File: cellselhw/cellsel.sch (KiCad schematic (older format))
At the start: 51 parts

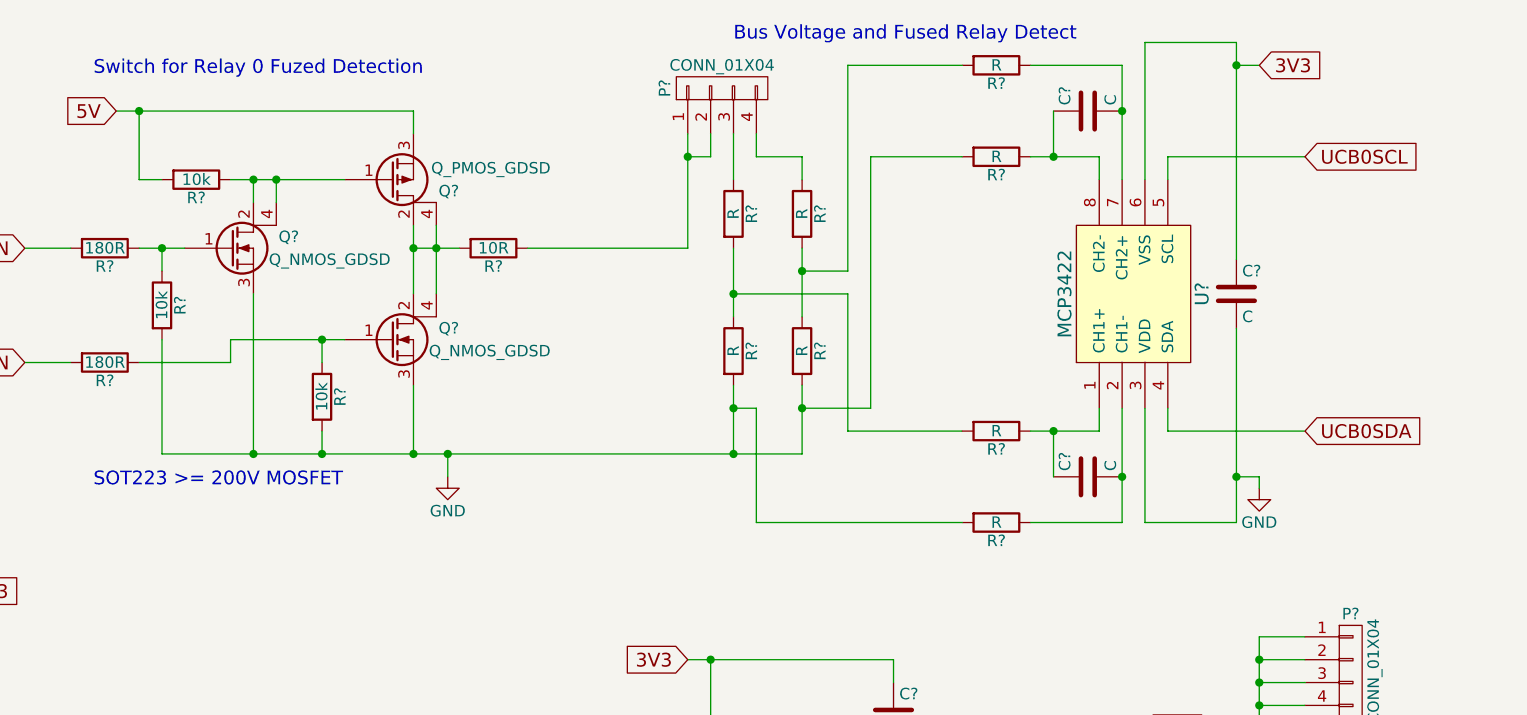
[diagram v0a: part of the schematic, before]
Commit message: Added bus discharge transistors
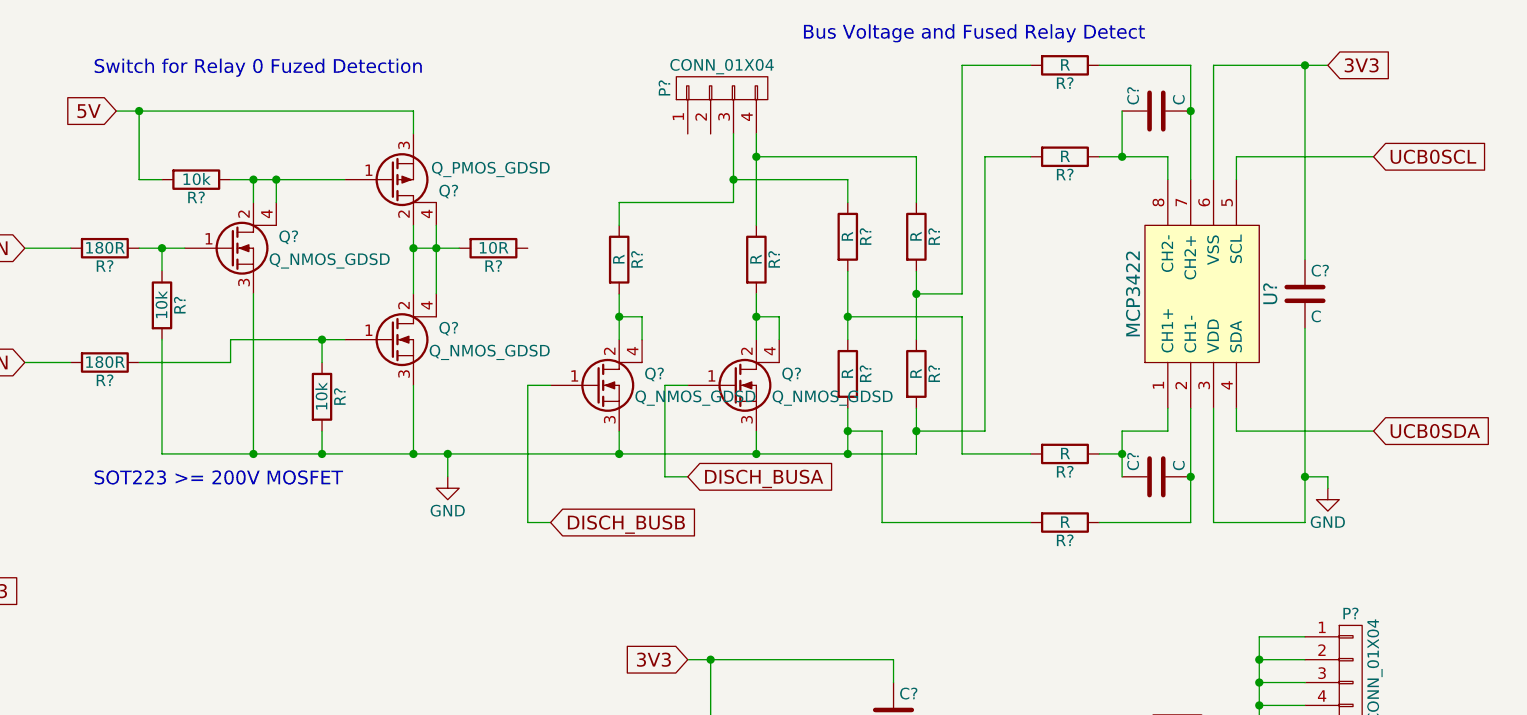
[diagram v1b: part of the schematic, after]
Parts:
- added Q? (x2): Q_NMOS_GDSD, symbol Q_NMOS_GDSD
- added R? (x2): R, symbol R
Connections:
- net GND: now also Q?.3 (S), Q?.3 (S)
- net at P?.3 (P3), R?.1: now also R?.1
- net at P?.4 (P4), R?.1: now also R?.1
- new net: Q?.2 (D), Q?.4 (D), R?.2 (x2)
- new net DISCH_BUSA: Q?.1 (G)
- new net DISCH_BUSB: Q?.1 (G)
- now unconnected: P?.1 (P1), P?.2 (P2), R?.1
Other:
- moved on the sheet: C?, R?, U?

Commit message: Schematic Complete
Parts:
- added P?: CONN_01X03, symbol CONN_01X03
- added P?: CONN_01X04, symbol CONN_01X04
- added R?: 4k7, symbol R
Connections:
- net 12V: now also P?.1 (P1), P?.2 (P2)
- net 3V3: now also P?.1 (P1), R?.1
- net DISCH_BUSA: now also U?.18 (P2.5)
- net DISCH_BUSB: now also U?.17 (P2.4)
- net GND: now also P?.3 (P3), P?.3 (P3), P?.4 (P4)
- net at U?.16 (P2.3): now also P?.2 (P2), R?.2
- net at R?.1: now also P?.1 (P1), P?.2 (P2)
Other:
- note added: "DS18B20"
- note added: "NCH SOT223 FET: IRLL110BPF (100V) / STN4NF20L (200V)\nPCH SOT223 FET: BSP220,115 (-220V)"
- moved on the sheet: C?, U?

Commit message: PCB Layout Stage 1
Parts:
- added C13: 100uF, Capacitors_SMD:C_1206, symbol CP1
- C1, C8: renamed from C?; value C -> 100nF; footprint (none) -> Capacitors_SMD:C_0603
- C10, C11: renamed from C?; footprint (none) -> Capacitors_SMD:C_0603
- C12, C14, C15, C5: renamed from C?; value C -> 1uF; footprint (none) -> Capacitors_SMD:C_0805
- C2: renamed from C?; footprint (none) -> Capacitors_SMD:C_1210
- C3, C4, C6, C7: renamed from C?; footprint (none) -> Capacitors_SMD:C_1206
- C9: renamed from C?; footprint (none) -> Capacitors_SMD:C_0805
- D1: renamed from D?; footprint (none) -> TO_SOT_Packages_SMD:SOT-23
- P1, P2, P3, P4, P8: renamed from P?; footprint (none) -> Connectors_Molex:Molex_KK-6410-04_04x2.54mm_Straight
- P5, P6: renamed from P?; footprint (none) -> Connectors_Molex:Molex_KK-6410-08_08x2.54mm_Straight
- P7: renamed from P?; footprint (none) -> Connectors_Molex:Molex_KK-6410-03_03x2.54mm_Straight
- Q1, Q2, Q3, Q4, Q5: renamed from Q?; footprint (none) -> TO_SOT_Packages_SMD:SOT-223
- R1, R15, R16, R2: renamed from R?; value R -> 10k; footprint (none) -> Resistors_SMD:R_0603
- R10, R11, R14, R17, R18, R19, R20, R21, R22, R3, R6: renamed from R?; footprint (none) -> Resistors_SMD:R_0603
- R12, R13: renamed from R?; value R -> 10k; footprint (none) -> RES_TH:PRECISION_RESISTOR_5MM
- R4, R5: renamed from R?; value R -> 500k; footprint (none) -> RES_TH:PRECISION_RESISTOR_5MM
- R7: renamed from R?; footprint (none) -> Resistors_SMD:R_0805
- R8, R9: renamed from R?; value R -> 1k; footprint (none) -> Resistors_SMD:R_0805
- U1, U3: renamed from U?; footprint (none) -> TO_SOT_Packages_SMD:SOT-223
- U2: renamed from U?; footprint (none) -> Housings_SOIC:SOIC-8_3.9x4.9mm_Pitch1.27mm
- U4: renamed from U?; footprint (none) -> Housings_SSOP:TSSOP-28_4.4x9.7mm_Pitch0.65mm
- U5, U7: renamed from U?; footprint (none) -> Housings_DIP:DIP-18_W7.62mm
- U6: renamed from U?; footprint (none) -> Housings_SOIC:SOIC-28W_7.5x17.9mm_Pitch1.27mm
- U8: renamed from U?; footprint (none) -> Housings_SOIC:SOIC-16W_7.5x10.3mm_Pitch1.27mm
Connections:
- net 12V: now also C13.1
- net GND: now also C13.2

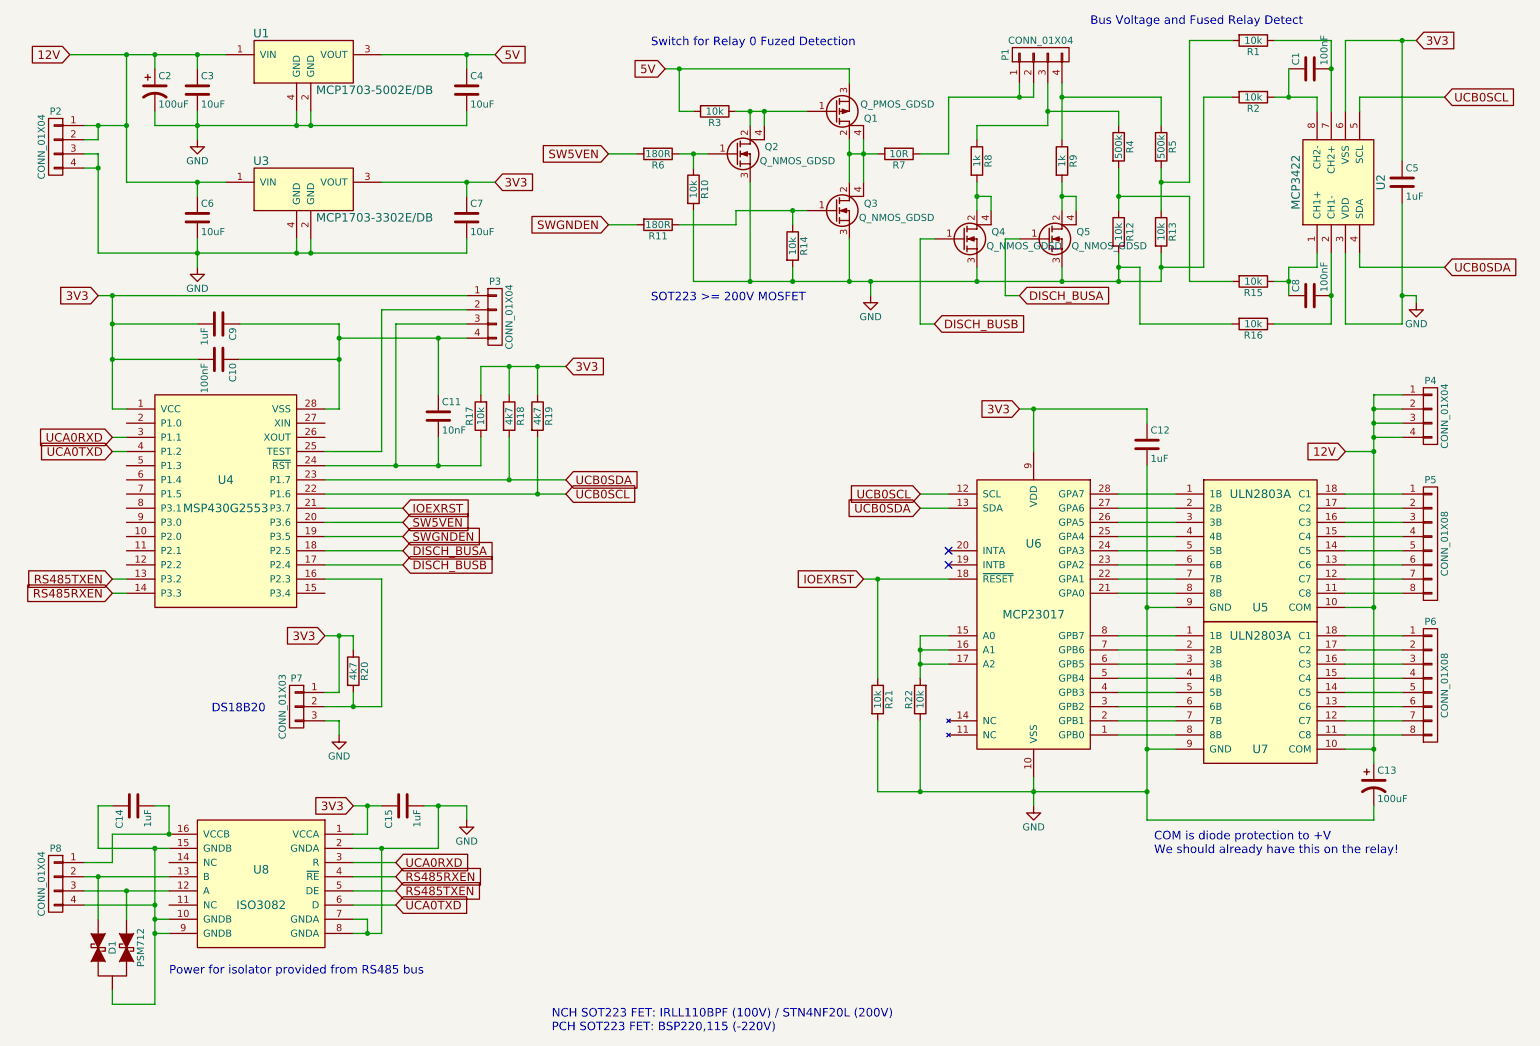
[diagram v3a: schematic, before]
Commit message: Finalused Transistor Selection
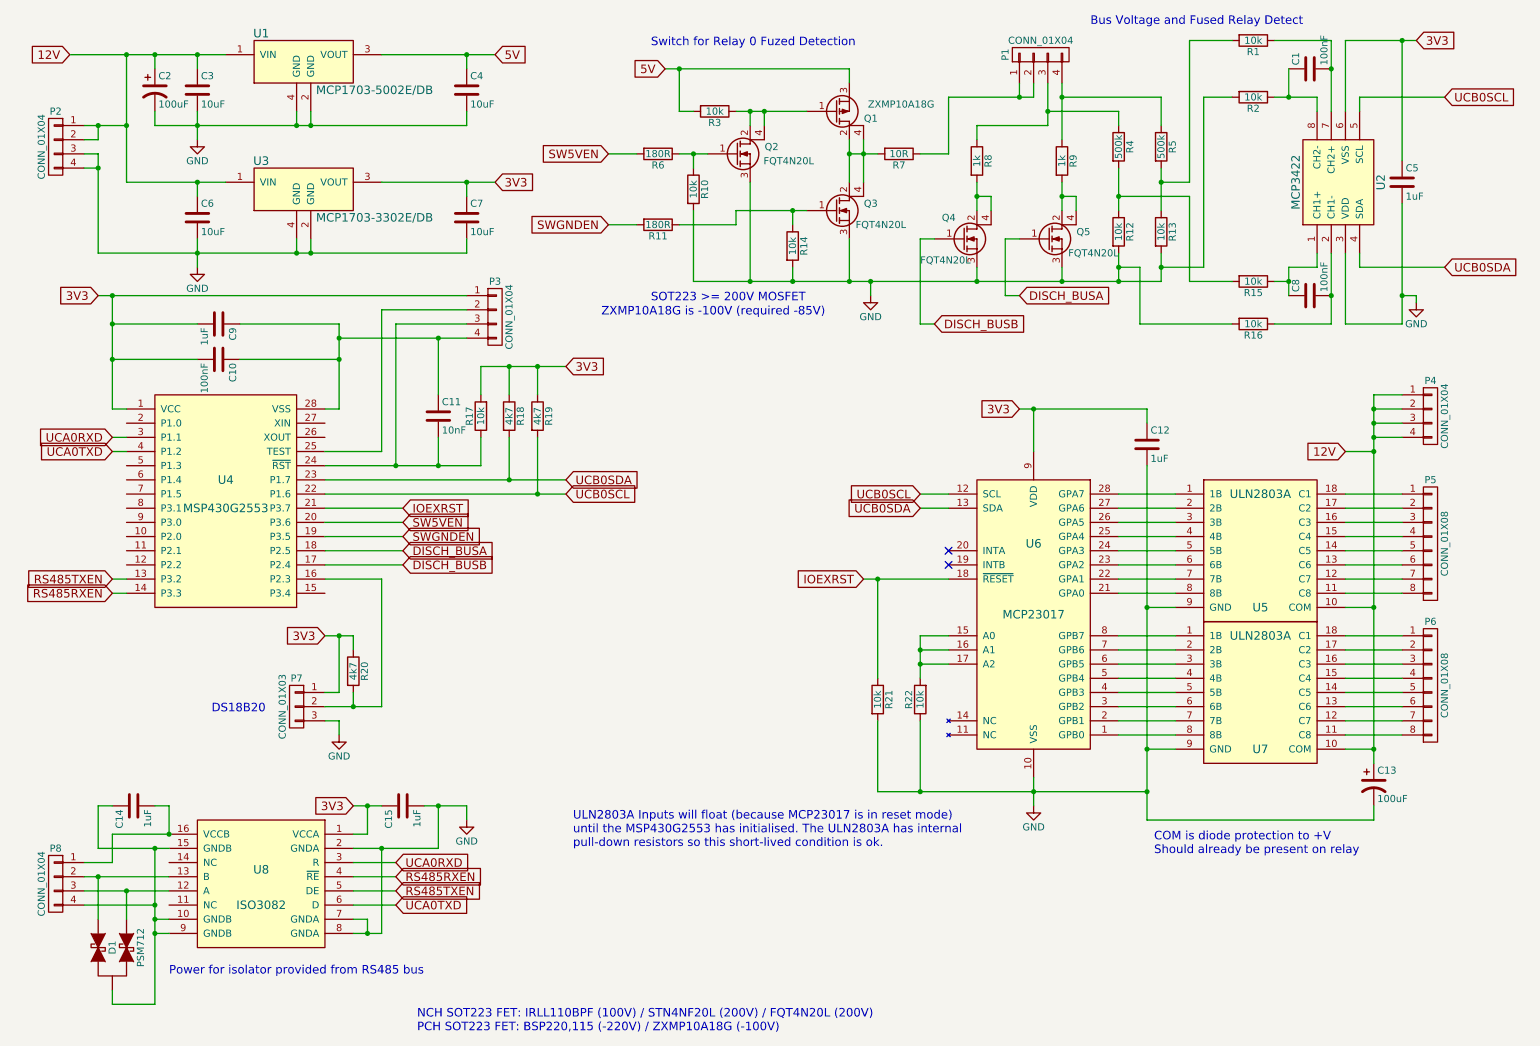
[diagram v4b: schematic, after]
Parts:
- Q1: value Q_PMOS_GDSD -> ZXMP10A18G
- Q2, Q3, Q4, Q5: value Q_NMOS_GDSD -> FQT4N20L
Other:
- note added: "COM is diode protection to +V\nShould already be present on relay"
- note added: "NCH SOT223 FET: IRLL110BPF (100V) / STN4NF20L (200V) / FQT4N20L (200V)\nPCH SOT223 FET: BSP220,115 (-220V) / ZXMP10A18G (-100V)"
- note added: "ULN2803A Inputs will float (because MCP23017 is in reset mode)\nuntil the MSP430G2553 has initialised. The ULN2803A has internal\npull-down resistors so this short-lived condition is ok."
- note added: "ZXMP10A18G is -100V (required -85V)"
- note removed: "COM is diode protection to +V\nWe should already have this on the relay!"
- note removed: "NCH SOT223 FET: IRLL110BPF (100V) / STN4NF20L (200V)\nPCH SOT223 FET: BSP220,115 (-220V)"
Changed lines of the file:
@@
 LIBS:contrib
 LIBS:valves
+LIBS:vreg
 LIBS:msp430
+LIBS:powerswitchics
+LIBS:ioexpanders
+LIBS:adcanddac
+LIBS:ti
+LIBS:transientsuppressor
 LIBS:cellsel-cache
 EELAYER 25 0
@@
 P 5500 1500
 F 0 "Q2" H 5800 1550 50  0000 R CNN
-F 1 "Q_NMOS_GDSD" H 6200 1450 50  0000 R CNN
+F 1 "FQT4N20L" H 6050 1450 50  0000 R CNN
 F 2 "TO_SOT_Packages_SMD:SOT-223" H 5700 1600 50  0001 C CNN
 F 3 "" H 5500 1500 50  0000 C CNN
@@
 P 6200 1900
 F 0 "Q3" H 6500 1950 50  0000 R CNN
-F 1 "Q_NMOS_GDSD" H 6900 1850 50  0000 R CNN
+F 1 "FQT4N20L" H 6700 1800 50  0000 R CNN
 F 2 "TO_SOT_Packages_SMD:SOT-223" H 6400 2000 50  0001 C CNN
 F 3 "" H 6200 1900 50  0000 C CNN
@@
 P 6200 1200
 F 0 "Q1" H 6500 1250 50  0000 R CNN
-F 1 "Q_PMOS_GDSD" H 6900 1150 50  0000 R CNN
+F 1 "ZXMP10A18G" H 6900 1150 50  0000 R CNN
 F 2 "TO_SOT_Packages_SMD:SOT-223" H 6400 1300 50  0001 C CNN
 F 3 "" H 6200 1200 50  0000 C CNN
@@
 Connection ~ 7600 3300
 Text Notes 8450 6450 0    60   ~ 0
-COM is diode protection to +V\nWe should already have this on the relay!
+COM is diode protection to +V\nShould already be present on relay
 Text GLabel 2800 6100 0    60   Input ~ 0
 3V3
@@
 U 1 1 5A7CCD8E
 P 7100 2100
-F 0 "Q4" H 7400 2150 50  0000 R CNN
-F 1 "Q_NMOS_GDSD" H 7800 2050 50  0000 R CNN
+F 0 "Q4" H 7050 2250 50  0000 R CNN
+F 1 "FQT4N20L" H 6800 1950 50  0000 L CNN
 F 2 "TO_SOT_Packages_SMD:SOT-223" H 7300 2200 50  0001 C CNN
 F 3 "" H 7100 2100 50  0000 C CNN
@@
 P 7700 2100
 F 0 "Q5" H 8000 2150 50  0000 R CNN
-F 1 "Q_NMOS_GDSD" H 8400 2050 50  0000 R CNN
+F 1 "FQT4N20L" H 8200 2000 50  0000 R CNN
 F 2 "TO_SOT_Packages_SMD:SOT-223" H 7900 2200 50  0001 C CNN
 F 3 "" H 7700 2100 50  0000 C CNN
@@
 Wire Wire Line
 	10200 700  10200 1550
-Text Notes 4200 7700 0    60   ~ 0
-NCH SOT223 FET: IRLL110BPF (100V) / STN4NF20L (200V)\nPCH SOT223 FET: BSP220,115 (-220V)
+Text Notes 3250 7700 0    60   ~ 0
+NCH SOT223 FET: IRLL110BPF (100V) / STN4NF20L (200V) / FQT4N20L (200V)\nPCH SOT223 FET: BSP220,115 (-220V) / ZXMP10A18G (-100V)
 Text GLabel 3150 4300 2    60   Input ~ 0
 DISCH_BUSA
@@
 Connection ~ 8400 6000
 Connection ~ 10000 5700
+Text Notes 4550 2650 0    60   ~ 0
+ZXMP10A18G is -100V (required -85V)
+Text Notes 4350 6400 0    60   ~ 0
+ULN2803A Inputs will float (because MCP23017 is in reset mode)\nuntil the MSP430G2553 has initialised. The ULN2803A has internal\npull-down resistors so this short-lived condition is ok.
 $EndSCHEMATC
